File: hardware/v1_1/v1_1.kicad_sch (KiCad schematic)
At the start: 78 parts, among them J1 AUDIO IN, J2 MIDI OUT, J3 MIDI IN, J4 MIDI THRU, J5 OUTPUT R, J6 OUTPUT L - MONO, J7 EXP 2, J8 EXP 1, J9 Batt In, SW1 RotaryEncoder_Switch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

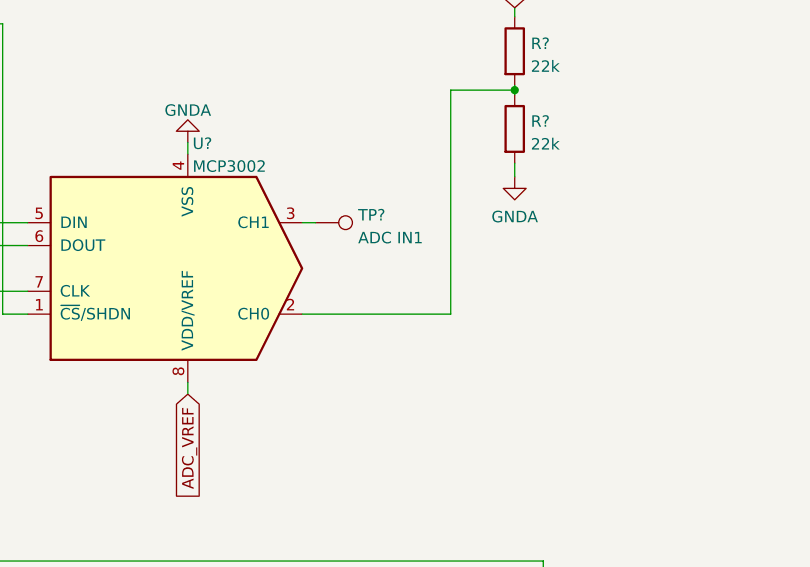
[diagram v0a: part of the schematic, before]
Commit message: Added connector for additionnal sensor
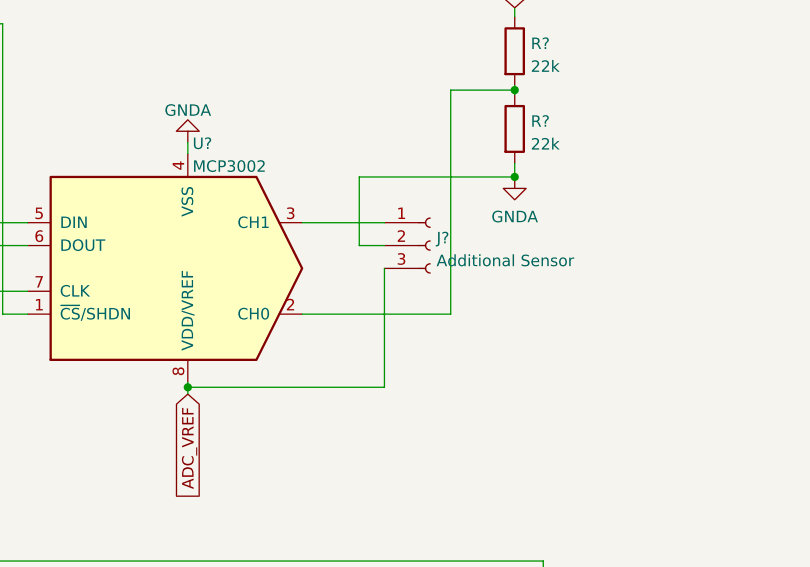
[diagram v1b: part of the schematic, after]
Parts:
- removed TP?: ADC IN1, symbol Connector:TestPoint
- added J?: Additional Sensor, symbol Connector:Conn_01x03_Female
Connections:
- net ADC_VREF: now also J?.3 (Pin_3)
- net GNDA: now also J?.2 (Pin_2)
- net at U?.3 (CH1): now also J?.1 (Pin_1)
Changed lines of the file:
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@@
   (junction (at 424.18 113.665) (diameter 0) (color 0 0 0 0)
   )
+  (junction (at 235.458 93.726) (diameter 0) (color 0 0 0 0)
+  )
   (junction (at 163.195 30.48) (diameter 0) (color 0 0 0 0)
   )
@@
   (junction (at 159.385 86.36) (diameter 0) (color 0 0 0 0)
   )
+  (junction (at 271.78 70.358) (diameter 0) (color 0 0 0 0)
+  )
   (junction (at 167.005 30.48) (diameter 0) (color 0 0 0 0)
   )
@@
     (stroke (width 0) (type default) (color 0 0 0 0))
   )
+  (wire (pts (xy 254.508 70.358) (xy 254.508 77.978))
+    (stroke (width 0) (type default) (color 0 0 0 0))
+  )
   (wire (pts (xy 419.1 50.8) (xy 403.86 50.8))
     (stroke (width 0) (type default) (color 0 0 0 0))
@@
     (stroke (width 0) (type default) (color 0 0 0 0))
   )
-  (wire (pts (xy 271.78 68.834) (xy 271.78 70.358))
-    (stroke (width 0) (type default) (color 0 0 0 0))
-  )
   (polyline (pts (xy 17.78 162.56) (xy 17.78 193.675))
     (stroke (width 0) (type default) (color 0 0 0 0))
@@
     (stroke (width 0) (type default) (color 0 0 0 0))
   )
+  (wire (pts (xy 257.302 77.978) (xy 254.508 77.978))
+    (stroke (width 0) (type default) (color 0 0 0 0))
+  )
   (wire (pts (xy 136.144 77.47) (xy 101.6 77.47))
     (stroke (width 0) (type default) (color 0 0 0 0))
@@
     (stroke (width 0) (type default) (color 0 0 0 0))
   )
-  (wire (pts (xy 248.158 75.438) (xy 249.682 75.438))
+  (wire (pts (xy 248.158 75.438) (xy 257.302 75.438))
     (stroke (width 0) (type default) (color 0 0 0 0))
   )
@@
     (stroke (width 0) (type default) (color 0 0 0 0))
   )
-  (wire (pts (xy 235.458 93.218) (xy 235.458 94.488))
+  (wire (pts (xy 235.458 93.726) (xy 235.458 94.488))
+    (stroke (width 0) (type default) (color 0 0 0 0))
+  )
+  (wire (pts (xy 235.458 93.218) (xy 235.458 93.726))
     (stroke (width 0) (type default) (color 0 0 0 0))
   )
@@
     (stroke (width 0) (type default) (color 0 0 0 0))
   )
+  (wire (pts (xy 271.78 68.834) (xy 271.78 70.358))
+    (stroke (width 0) (type default) (color 0 0 0 0))
+  )
   (wire (pts (xy 255.27 134.62) (xy 255.905 134.62))
     (stroke (width 0) (type default) (color 0 0 0 0))
@@
     (stroke (width 0) (type default) (color 0 0 0 0))
   )
+  (wire (pts (xy 235.458 93.726) (xy 257.302 93.726))
+    (stroke (width 0) (type default) (color 0 0 0 0))
+  )
   (wire (pts (xy 26.035 92.71) (xy 26.035 158.75))
     (stroke (width 0) (type default) (color 0 0 0 0))
@@
     (stroke (width 0) (type default) (color 0 0 0 0))
   )
+  (wire (pts (xy 257.302 93.726) (xy 257.302 80.518))
+    (stroke (width 0) (type default) (color 0 0 0 0))
+  )
   (wire (pts (xy 403.86 44.45) (xy 403.86 50.8))
     (stroke (width 0) (type default) (color 0 0 0 0))
@@
     (stroke (width 0) (type default) (color 0 0 0 0))
   )
+  (wire (pts (xy 254.508 70.358) (xy 271.78 70.358))
+    (stroke (width 0) (type default) (color 0 0 0 0))
+  )
   (wire (pts (xy 137.668 99.314) (xy 137.668 74.93))
     (stroke (width 0) (type default) (color 0 0 0 0))
@@
     (pin "8")
   )
-  (symbol (lib_id "Connector:TestPoint") (at 249.682 75.438 270) (unit 1)
-    (in_bom yes) (on_board yes) (fields_autoplaced)
-    (property "Reference" "TP?" (id 0) (at 254.381 74.6033 90)
-      (effects (font (size 1.27 1.27)) (justify left))
-    )
-    (property "Value" "ADC IN1" (id 1) (at 254.381 77.1402 90)
-      (effects (font (size 1.27 1.27)) (justify left))
-    )
-    (property "Footprint" "" (id 2) (at 249.682 80.518 0)
-      (effects (font (size 1.27 1.27)) hide)
-    )
-    (property "Datasheet" "~" (id 3) (at 249.682 80.518 0)
-      (effects (font (size 1.27 1.27)) hide)
-    )
-    (pin "1")
-  )
   (symbol (lib_id "Connector:DIN-5_180degree") (at 263.525 132.08 0) (mirror x) (unit 1)
     (in_bom yes) (on_board yes) (fields_autoplaced)
@@
     (pin "5")
   )
+  (symbol (lib_id "Connector:Conn_01x03_Female") (at 262.382 77.978 0) (unit 1)
+    (in_bom yes) (on_board yes) (fields_autoplaced)
+    (property "Reference" "J?" (id 0) (at 263.0932 77.1433 0)
+      (effects (font (size 1.27 1.27)) (justify left))
+    )
+    (property "Value" "Additional Sensor" (id 1) (at 263.0932 79.6802 0)
+      (effects (font (size 1.27 1.27)) (justify left))
+    )
+    (property "Footprint" "" (id 2) (at 262.382 77.978 0)
+      (effects (font (size 1.27 1.27)) hide)
+    )
+    (property "Datasheet" "~" (id 3) (at 262.382 77.978 0)
+      (effects (font (size 1.27 1.27)) hide)
+    )
+    (pin "1")
+    (pin "2")
+    (pin "3")
+  )
   (symbol (lib_id "power:+3V3") (at 54.61 105.41 90) (unit 1)
     (in_bom yes) (on_board yes) (fields_autoplaced)
@@
       (reference "J9") (unit 1) (value "Batt In") (footprint "Connector_JST:JST_XH_B2B-XH-A_1x02_P2.50mm_Vertical")
     )
+    (path "/b4ba5993-6d66-460b-bbf5-e03b75378bc3"
+      (reference "J?") (unit 1) (value "Additional Sensor") (footprint "")
+    )
     (path "/7aa8ebeb-8bea-4614-8ec6-7c790f165918"
       (reference "R1") (unit 1) (value "10") (footprint "Resistor_THT:R_Axial_DIN0207_L6.3mm_D2.5mm_P7.62mm_Horizontal")
@@
       (reference "SW2") (unit 1) (value "SW_SPDT") (footprint "Package_TO_SOT_THT:TO-126-3_Vertical")
     )
-    (path "/49706c26-c4c7-4204-9c3d-4ac0b358d591"
-      (reference "TP?") (unit 1) (value "ADC IN1") (footprint "")
-    )
     (path "/55be732d-d054-4d1b-b915-371f3d6eb5d0"

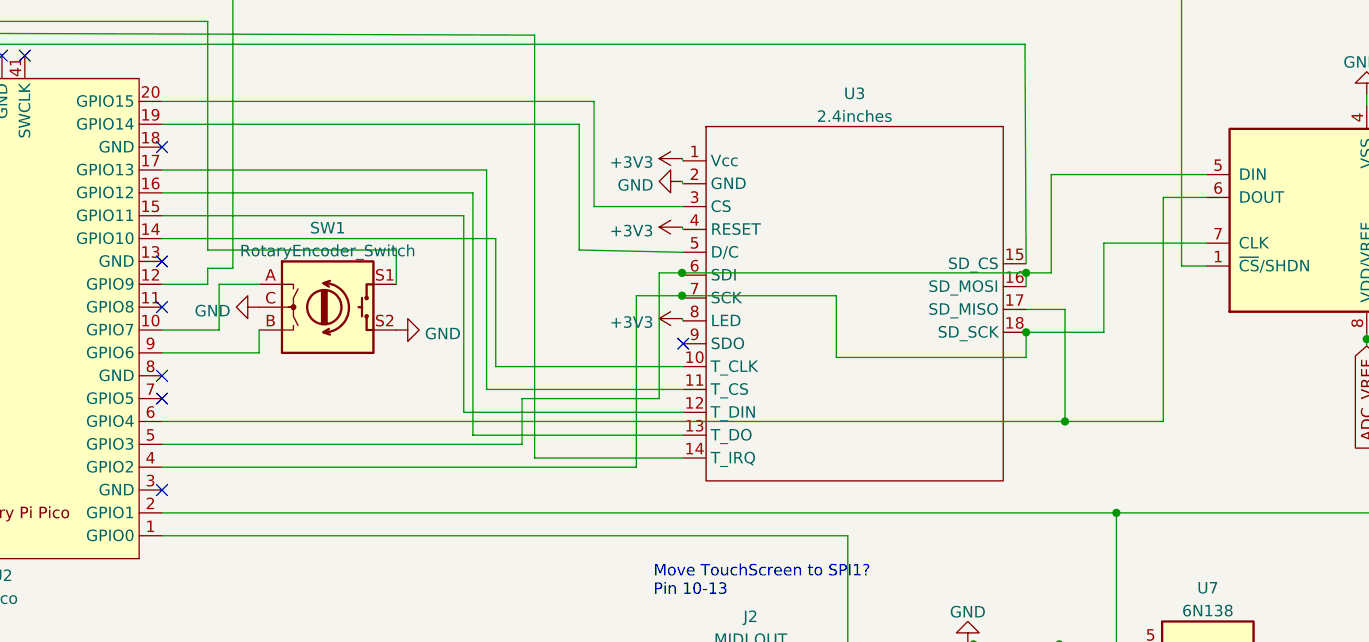
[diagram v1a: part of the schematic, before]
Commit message: Re-routed pcb for 1.1
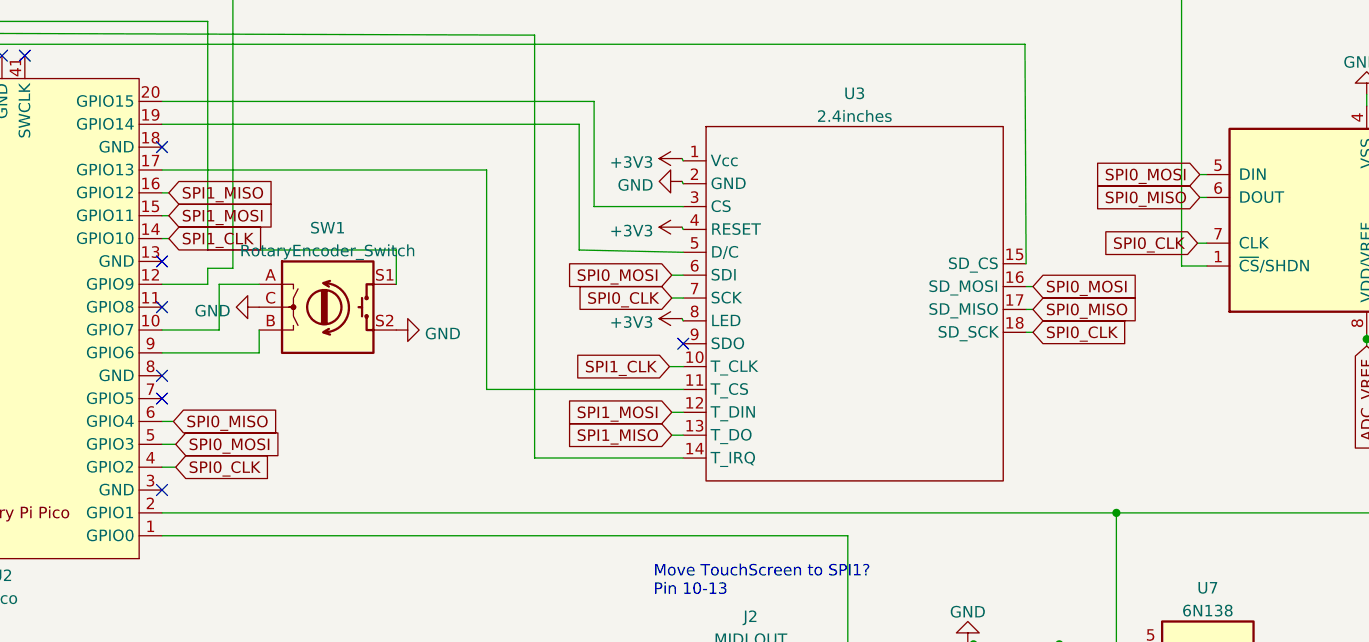
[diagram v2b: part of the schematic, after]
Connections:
- net SPI0_MOSI: now reaches U2.5 (GPIO3), U3.16 (SD_MOSI), U3.6 (SDI), U?.5 (DIN)
- net SPI0_MISO: now reaches U2.6 (GPIO4), U3.17 (SD_MISO), U?.6 (DOUT)
- net SPI0_CLK: now reaches U2.4 (GPIO2), U3.18 (SD_SCK), U3.7 (SCK), U?.7 (CLK)
- net SPI1_CLK: now reaches U2.14 (GPIO10), U3.10 (T_CLK)
- net SPI1_MOSI: now reaches U2.15 (GPIO11), U3.12 (T_DIN)
- net SPI1_MISO: now reaches U2.16 (GPIO12), U3.13 (T_DO)

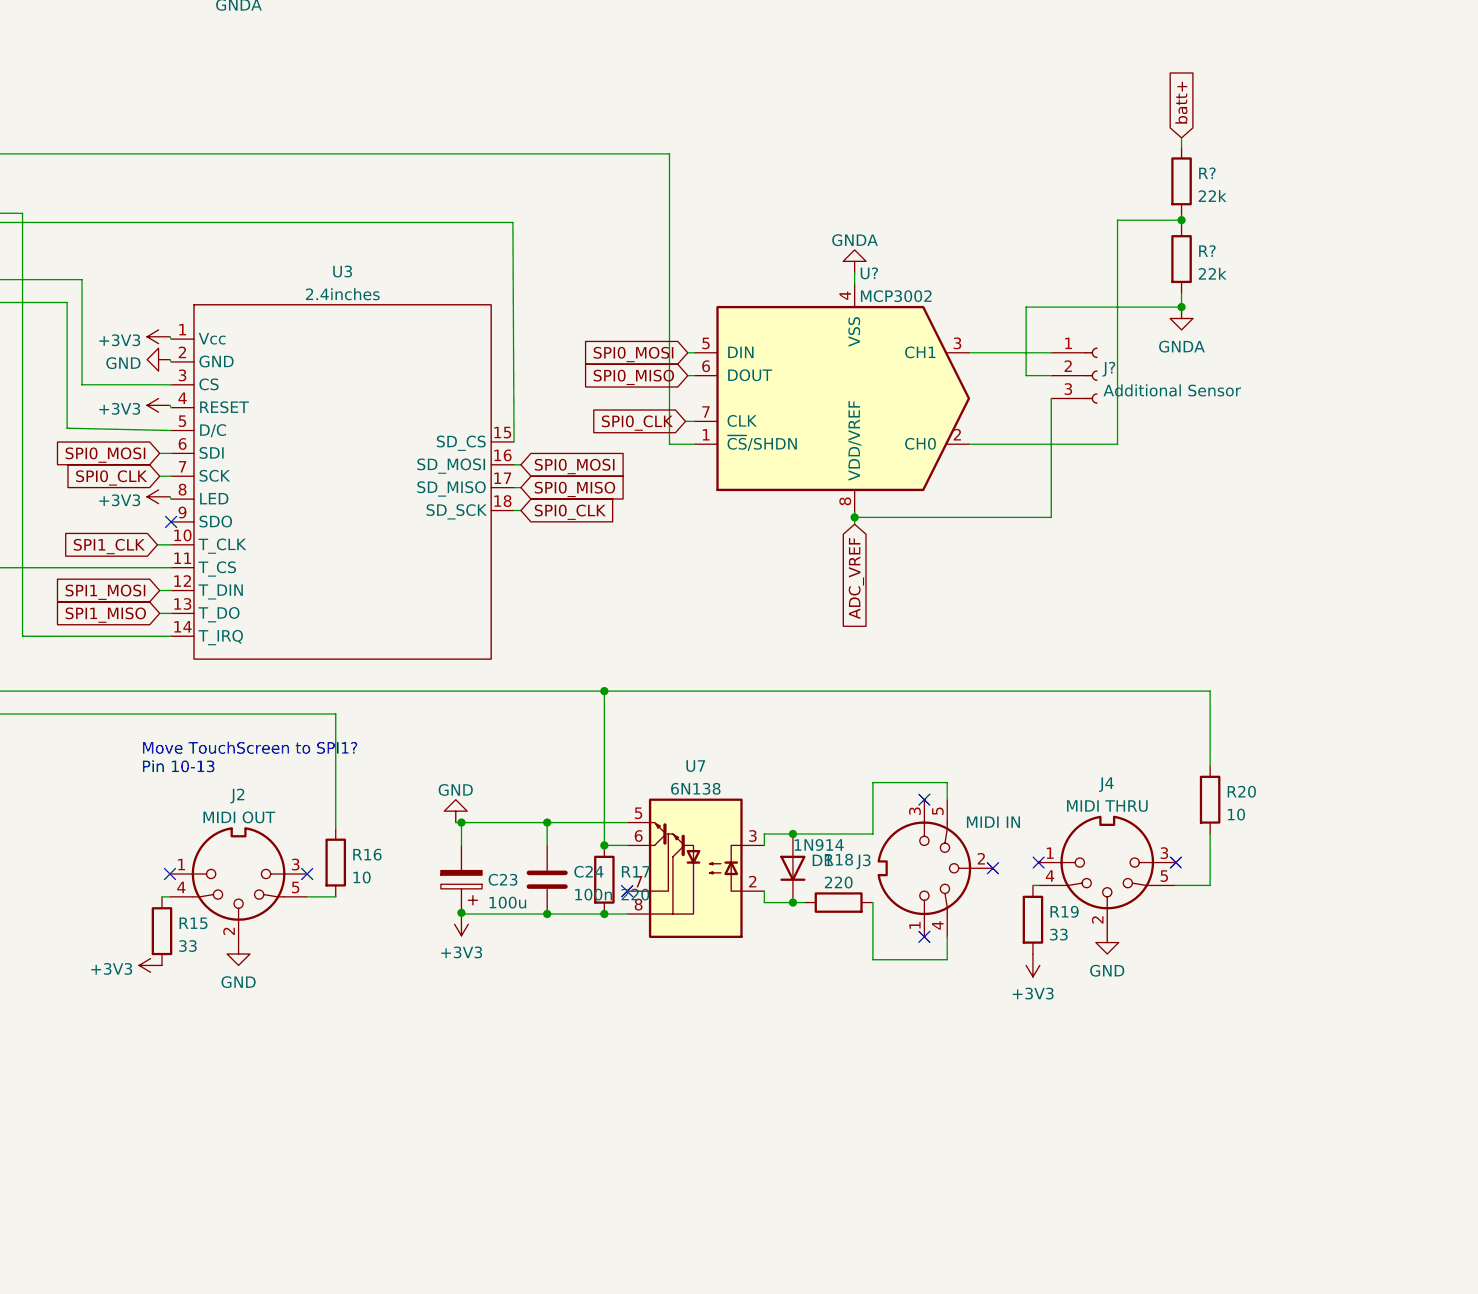
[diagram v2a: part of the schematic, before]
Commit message: Added MIDI over TRS connector
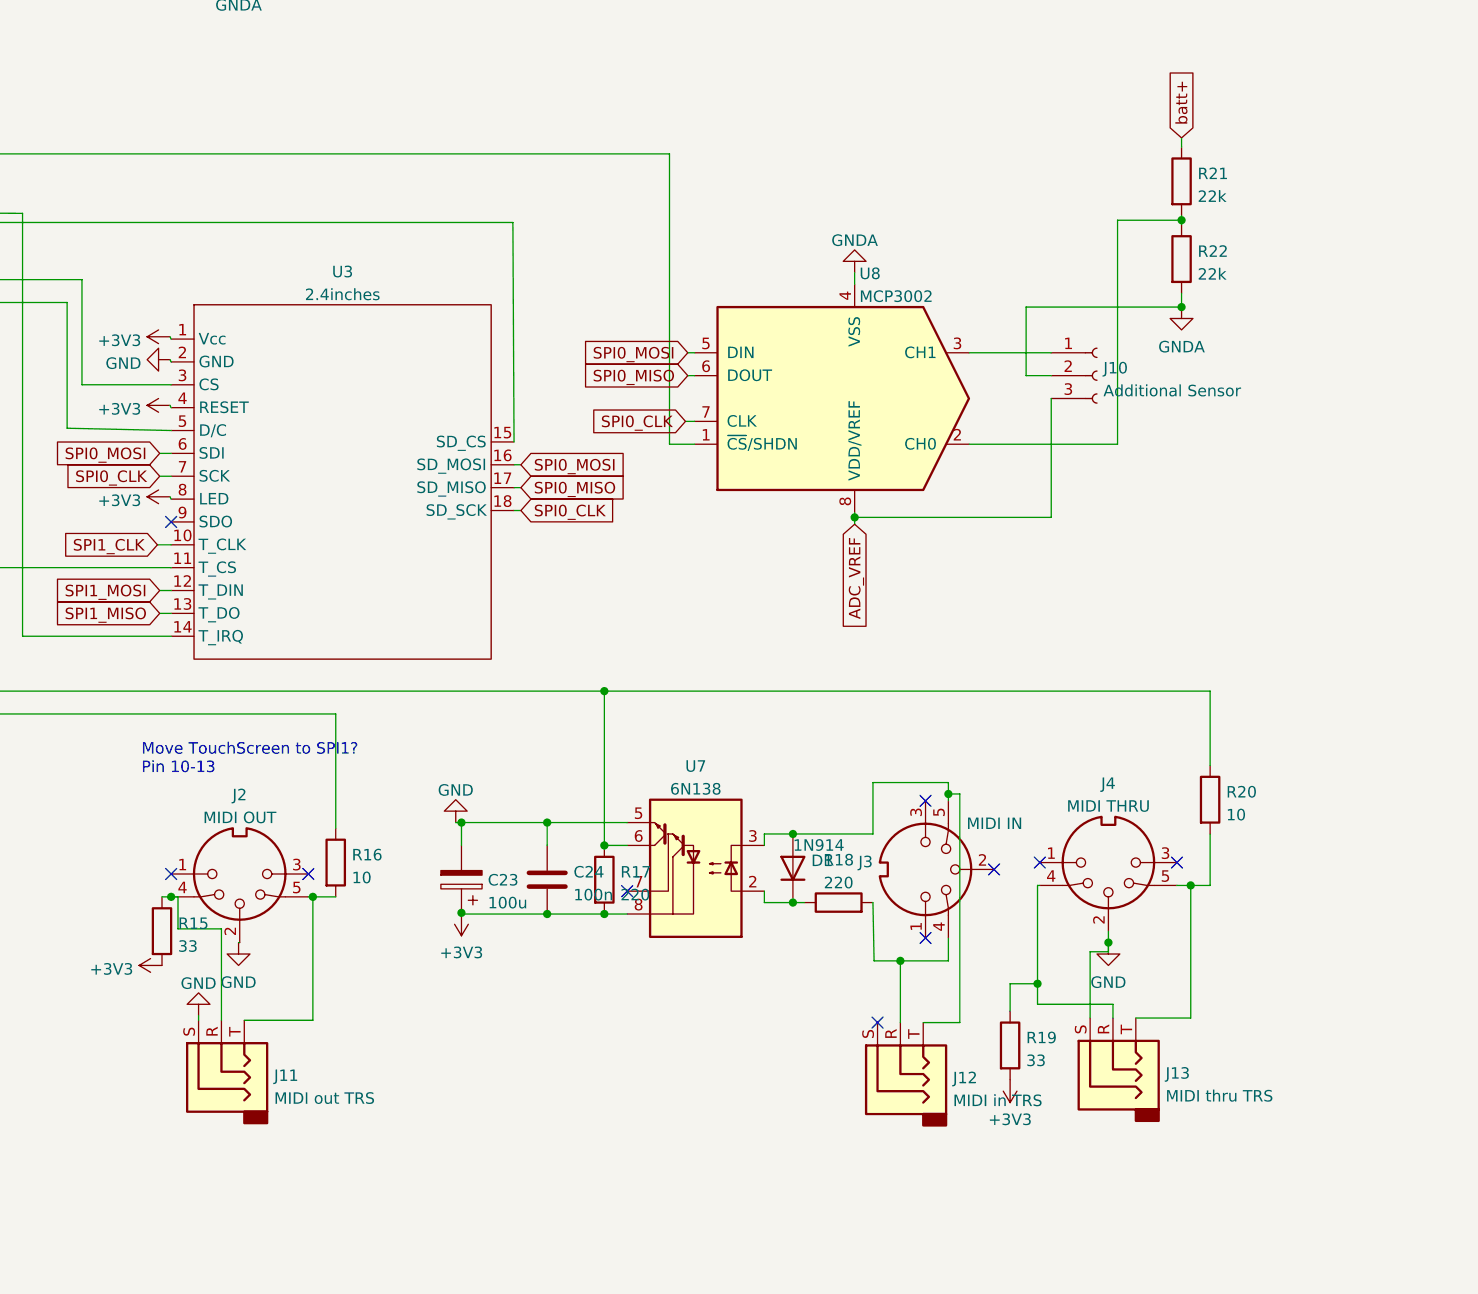
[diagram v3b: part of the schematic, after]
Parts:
- added J11: MIDI out TRS, MIDI_TRS:PJ-320B, symbol Connector:AudioJack3
- added J12: MIDI in TRS, MIDI_TRS:PJ-320B, symbol Connector:AudioJack3
- added J13: MIDI thru TRS, MIDI_TRS:PJ-320B, symbol Connector:AudioJack3
- J10: renamed from J?; footprint (none) -> Connector_JST:JST_PH_B3B-PH-K_1x03_P2.00mm_Vertical
- R21, R22: renamed from R?; footprint (none) -> Resistor_THT:R_Axial_DIN0207_L6.3mm_D2.5mm_P7.62mm_Horizontal
- U8: renamed from U?; footprint (none) -> Package_DIP:DIP-8_W7.62mm_Socket
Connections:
- net GND: now also J11.S, J13.S
- net at J4.4, R19.1: now also J13.R
- net at J3.4, R18.2: now also J12.R
- net at J4.5, R20.2: now also J13.T
- net at D1.2 (A), J3.5, U7.3 (C2): now also J12.T
- net at J2.4, R15.1: now also J11.R
- net at J2.5, R16.2: now also J11.T
- no-connect marks 42 -> 43
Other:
- moved on the sheet: R19
